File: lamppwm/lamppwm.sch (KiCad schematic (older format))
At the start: 15 parts, among them IC1 ATTINY85-S, P1 CONN_3X2, Q1 IRLML2246TRPBF, SW1 SWITCH-4, U1 AP7313

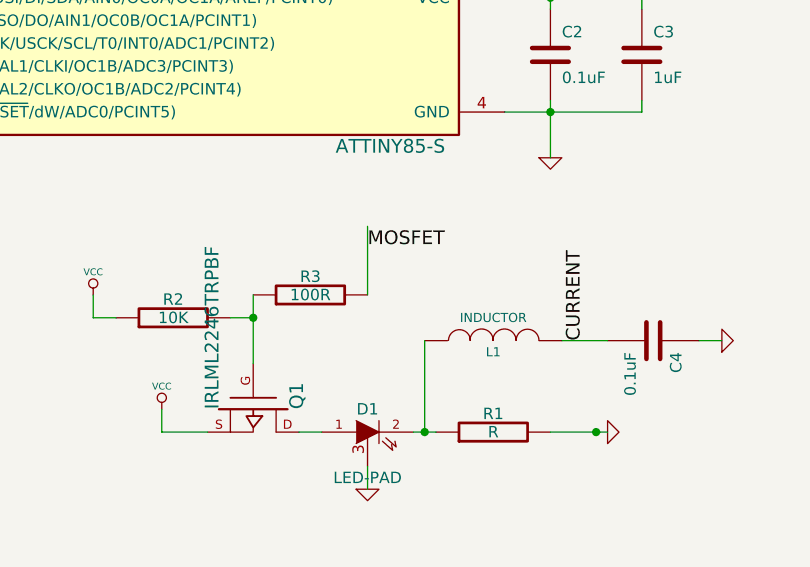
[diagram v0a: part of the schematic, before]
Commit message: lamppwm updates
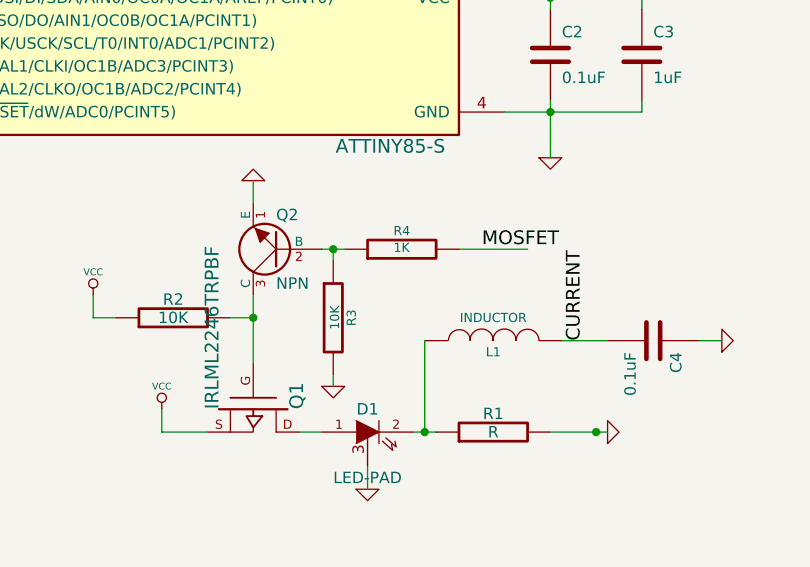
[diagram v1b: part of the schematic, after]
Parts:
- added Q2: NPN, ~, symbol NPN
- added R4: 1K, ~, symbol R
- R3: value 100R -> 10K; footprint (none) -> ~
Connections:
- wire segments 50 -> 54
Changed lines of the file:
@@
-EESchema Schematic File Version 2  date Thu 21 Feb 2013 10:03:48 AM EST
+EESchema Schematic File Version 2  date Mon 25 Feb 2013 07:26:33 PM EST
 LIBS:lamp
 LIBS:power
@@
 Sheet 1 1
 Title ""
-Date "21 feb 2013"
+Date "26 feb 2013"
 Rev ""
 Comp ""
@@
 CURRENT
 $Comp
-L R R3
-U 1 1 51094A11
-P 5550 3800
-F 0 "R3" V 5630 3800 50  0000 C CNN
-F 1 "100R" V 5550 3800 50  0000 C CNN
-F 2 "" H 5550 3800 60  0001 C CNN
-F 3 "" H 5550 3800 60  0001 C CNN
-	1    5550 3800
-	0    -1   -1   0
-$EndComp
-Wire Wire Line
-	5800 3800 5800 3500
-Text Label 5800 3600 0    60   ~ 0
-MOSFET
-$Comp
 L C C4
 U 1 1 51094D1E
@@
 Text Label 3000 2600 0    60   ~ 0
 BUTTON
+$Comp
+L NPN Q2
+U 1 1 512BFF81
+P 5400 3600
+F 0 "Q2" H 5400 3450 50  0000 R CNN
+F 1 "NPN" H 5400 3750 50  0000 R CNN
+F 2 "~" H 5400 3600 60  0000 C CNN
+F 3 "~" H 5400 3600 60  0000 C CNN
+	1    5400 3600
+	-1   0    0    1
+$EndComp
+$Comp
+L GND #PWR014
+U 1 1 512BFF9D
+P 5300 3300
+F 0 "#PWR014" H 5300 3300 30  0001 C CNN
+F 1 "GND" H 5300 3230 30  0001 C CNN
+F 2 "" H 5300 3300 60  0000 C CNN
+F 3 "" H 5300 3300 60  0000 C CNN
+	1    5300 3300
+	-1   0    0    1
+$EndComp
+Wire Wire Line
+	5300 3400 5300 3300
+$Comp
+L R R4
+U 1 1 512BFFE6
+P 5950 3600
+F 0 "R4" V 6030 3600 40  0000 C CNN
+F 1 "1K" V 5957 3601 40  0000 C CNN
+F 2 "~" V 5880 3600 30  0000 C CNN
+F 3 "~" H 5950 3600 30  0000 C CNN
+	1    5950 3600
+	0    -1   -1   0
+$EndComp
+Wire Wire Line
+	5600 3600 5700 3600
+Wire Wire Line
+	6200 3600 6500 3600
+Text Label 6300 3600 0    60   ~ 0
+MOSFET
+$Comp
+L R R3
+U 1 1 512C0193
+P 5650 3900
+F 0 "R3" V 5730 3900 40  0000 C CNN
+F 1 "10K" V 5657 3901 40  0000 C CNN
+F 2 "~" V 5580 3900 30  0000 C CNN
+F 3 "~" H 5650 3900 30  0000 C CNN
+	1    5650 3900
+	1    0    0    -1
+$EndComp
+$Comp
+L GND #PWR015
+U 1 1 512C01A2
+P 5650 4200
+F 0 "#PWR015" H 5650 4200 30  0001 C CNN
+F 1 "GND" H 5650 4130 30  0001 C CNN
+F 2 "" H 5650 4200 60  0000 C CNN
+F 3 "" H 5650 4200 60  0000 C CNN
+	1    5650 4200
+	1    0    0    -1
+$EndComp
+Wire Wire Line
+	5650 4200 5650 4150
+Wire Wire Line
+	5650 3650 5650 3600
+Connection ~ 5650 3600
 $EndSCHEMATC
